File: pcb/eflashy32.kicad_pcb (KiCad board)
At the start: 2 copper layers, 46.6 x 20.1 mm, 30 parts, among them J1 SERIAL, J2 10137062-00021LF, J3 SERIAL2, Q1 MMDT3904, SW1 JS202011CQN, U1 USBLC6-2SC6, U2 CP2102N-A02-GQFN24, U3 TLV75533PDBV

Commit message: prejig
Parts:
- D4: value POWER -> PWR

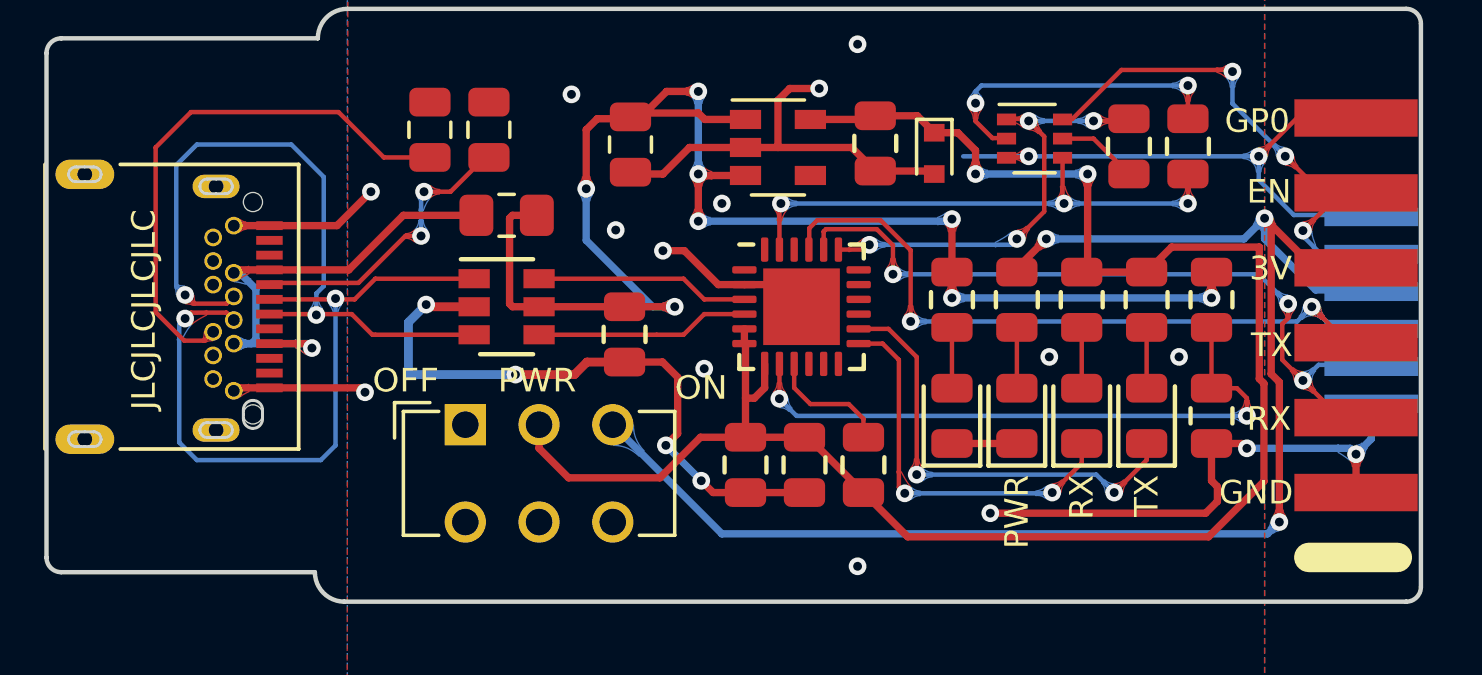
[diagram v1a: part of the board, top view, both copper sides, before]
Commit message: change to 4 line
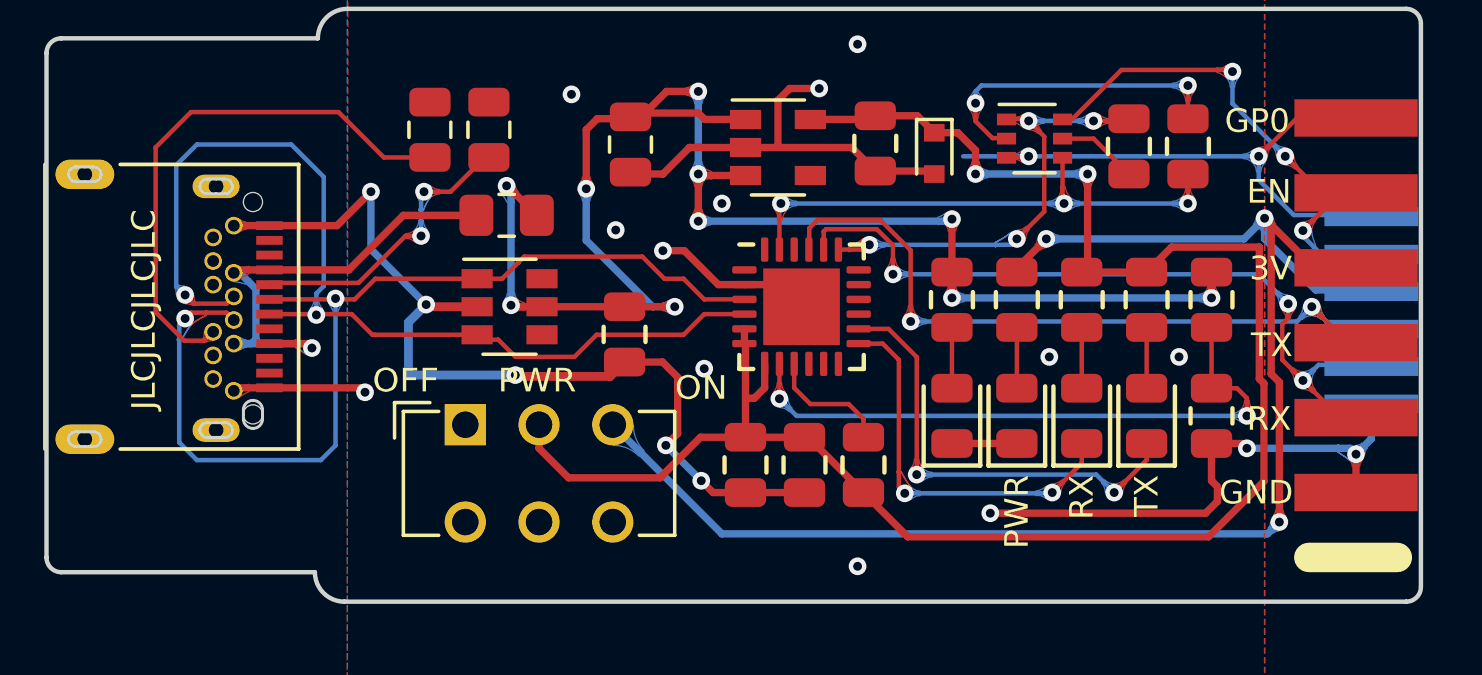
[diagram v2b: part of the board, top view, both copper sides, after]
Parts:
- F2: value 0ZCK0050AF2E (TLC-PSMD050) -> 0ZCK0050FF2E (TLC-PSMD050)
- R17: value 1k -> 5k1
- U1: value USBLC6-2SC6 -> ESD PROTECTION
- moved U1 0.10 mm to (96.1, 39.0)
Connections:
- U1 pad 4: /DOUT- -> (no net)
- U1 pad 6: /DOUT+ -> (no net)
- U2 pad 3: /DOUT+ -> /DIN+
- U2 pad 4: /DOUT- -> /DIN-
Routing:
- net /DIN+: track 24.4 -> 34.1 mm
- net /DIN-: track 24.7 -> 34.1 mm
- net /DOUT-: track 7.25 -> 0.00 mm
- net /DOUT+: track 7.25 -> 0.00 mm
- net GND: track 71.1 -> 75.7 mm
- net VBUS: track 52.3 -> 54.0 mm, vias 8 -> 10

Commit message: update
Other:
- net class Default removed
- net class Power removed
